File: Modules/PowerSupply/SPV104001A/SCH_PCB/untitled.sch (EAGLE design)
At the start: 24 parts, among them X2 SROUB3M, X3 SROUB3M, X4 SROUB3M, X5 SROUB3M

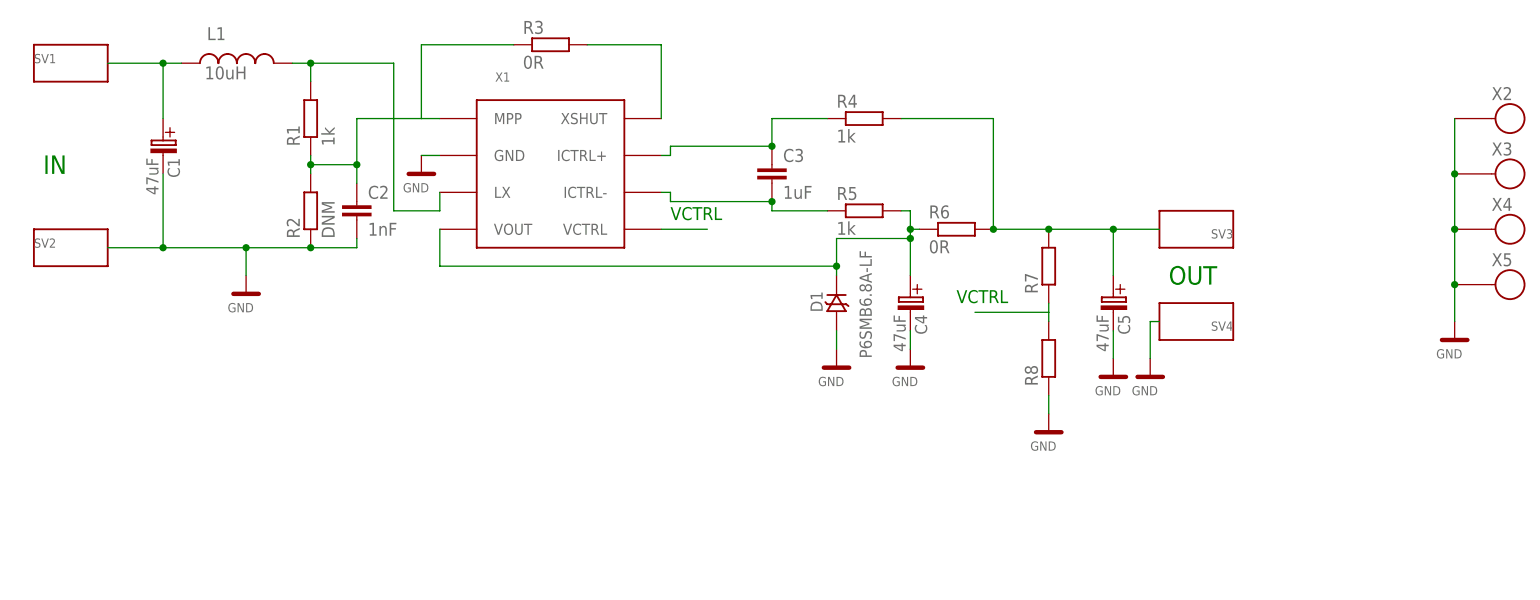
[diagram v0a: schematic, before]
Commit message: 
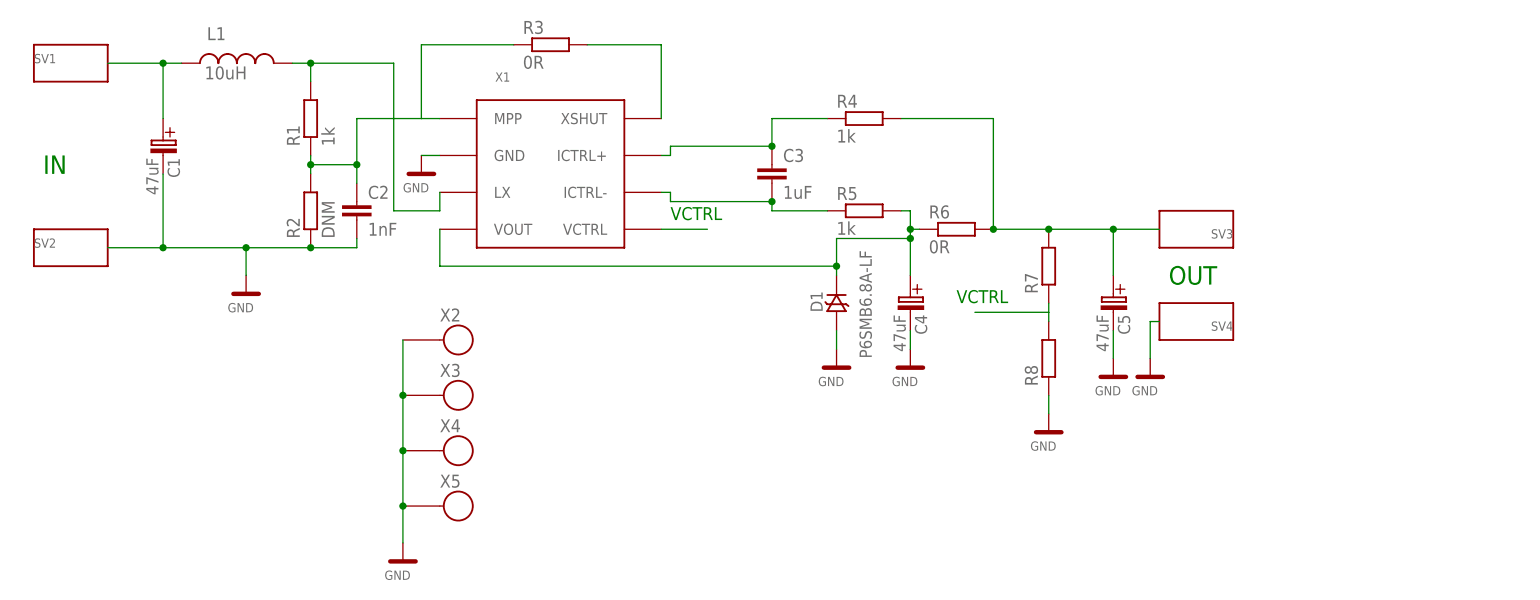
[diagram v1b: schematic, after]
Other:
- moved on the sheet: X2, X3, X4, X5
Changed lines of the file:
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@@
 <setting verticaltext="up"/>
 </settings>
-<grid distance="0.05" unitdist="inch" unit="inch" style="lines" multiple="1" display="no" altdistance="0.01" altunitdist="inch" altunit="inch"/>
+<grid distance="0.1" unitdist="inch" unit="inch" style="lines" multiple="1" display="no" altdistance="0.01" altunitdist="inch" altunit="inch"/>
 <layers>
-<layer number="1" name="Top" color="4" fill="1" visible="yes" active="no"/>
-<layer number="16" name="Bottom" color="1" fill="1" visible="yes" active="no"/>
-<layer number="17" name="Pads" color="2" fill="1" visible="yes" active="no"/>
-<layer number="18" name="Vias" color="2" fill="1" visible="yes" active="no"/>
-<layer number="19" name="Unrouted" color="6" fill="1" visible="yes" active="no"/>
-<layer number="20" name="Dimension" color="15" fill="1" visible="yes" active="no"/>
-<layer number="21" name="tPlace" color="7" fill="1" visible="yes" active="no"/>
-<layer number="22" name="bPlace" color="7" fill="1" visible="yes" active="no"/>
-<layer number="23" name="tOrigins" color="15" fill="1" visible="yes" active="no"/>
-<layer number="24" name="bOrigins" color="15" fill="1" visible="yes" active="no"/>
-<layer number="25" name="tNames" color="7" fill="1" visible="yes" active="no"/>
-<layer number="26" name="bNames" color="7" fill="1" visible="yes" active="no"/>
-<layer number="27" name="tValues" color="7" fill="1" visible="yes" active="no"/>
-<layer number="28" name="bValues" color="7" fill="1" visible="yes" active="no"/>
+<layer number="1" name="Top" color="4" fill="1" visible="no" active="no"/>
+<layer number="16" name="Bottom" color="1" fill="1" visible="no" active="no"/>
+<layer number="17" name="Pads" color="2" fill="1" visible="no" active="no"/>
+<layer number="18" name="Vias" color="2" fill="1" visible="no" active="no"/>
+<layer number="19" name="Unrouted" color="6" fill="1" visible="no" active="no"/>
+<layer number="20" name="Dimension" color="15" fill="1" visible="no" active="no"/>
+<layer number="21" name="tPlace" color="7" fill="1" visible="no" active="no"/>
+<layer number="22" name="bPlace" color="7" fill="1" visible="no" active="no"/>
+<layer number="23" name="tOrigins" color="15" fill="1" visible="no" active="no"/>
+<layer number="24" name="bOrigins" color="15" fill="1" visible="no" active="no"/>
+<layer number="25" name="tNames" color="7" fill="1" visible="no" active="no"/>
+<layer number="26" name="bNames" color="7" fill="1" visible="no" active="no"/>
+<layer number="27" name="tValues" color="7" fill="1" visible="no" active="no"/>
+<layer number="28" name="bValues" color="7" fill="1" visible="no" active="no"/>
 <layer number="29" name="tStop" color="7" fill="3" visible="no" active="no"/>
 <layer number="30" name="bStop" color="7" fill="6" visible="no" active="no"/>
@@
 <layer number="35" name="tGlue" color="7" fill="4" visible="no" active="no"/>
 <layer number="36" name="bGlue" color="7" fill="5" visible="no" active="no"/>
-<layer number="37" name="tTest" color="7" fill="1" visible="yes" active="no"/>
-<layer number="38" name="bTest" color="7" fill="1" visible="yes" active="no"/>
+<layer number="37" name="tTest" color="7" fill="1" visible="no" active="no"/>
+<layer number="38" name="bTest" color="7" fill="1" visible="no" active="no"/>
 <layer number="39" name="tKeepout" color="4" fill="11" visible="no" active="no"/>
 <layer number="40" name="bKeepout" color="1" fill="11" visible="no" active="no"/>
@@
 <layer number="44" name="Drills" color="7" fill="1" visible="no" active="no"/>
 <layer number="45" name="Holes" color="7" fill="1" visible="no" active="no"/>
-<layer number="46" name="Milling" color="3" fill="1" visible="yes" active="no"/>
-<layer number="47" name="Measures" color="7" fill="1" visible="yes" active="no"/>
-<layer number="48" name="Document" color="7" fill="1" visible="yes" active="no"/>
-<layer number="49" name="Reference" color="7" fill="1" visible="yes" active="no"/>
-<layer number="50" name="dxf" color="7" fill="1" visible="yes" active="no"/>
-<layer number="51" name="tDocu" color="7" fill="1" visible="yes" active="no"/>
-<layer number="52" name="bDocu" color="7" fill="1" visible="yes" active="no"/>
-<layer number="53" name="tPadExt" color="7" fill="1" visible="yes" active="no"/>
-<layer number="54" name="bPadExt" color="1" fill="1" visible="yes" active="no"/>
-<layer number="56" name="wert" color="7" fill="1" visible="yes" active="no"/>
+<layer number="46" name="Milling" color="3" fill="1" visible="no" active="no"/>
+<layer number="47" name="Measures" color="7" fill="1" visible="no" active="no"/>
+<layer number="48" name="Document" color="7" fill="1" visible="no" active="no"/>
+<layer number="49" name="Reference" color="7" fill="1" visible="no" active="no"/>
+<layer number="50" name="dxf" color="7" fill="1" visible="no" active="no"/>
+<layer number="51" name="tDocu" color="7" fill="1" visible="no" active="no"/>
+<layer number="52" name="bDocu" color="7" fill="1" visible="no" active="no"/>
+<layer number="53" name="tPadExt" color="7" fill="1" visible="no" active="no"/>
+<layer number="54" name="bPadExt" color="1" fill="1" visible="no" active="no"/>
+<layer number="56" name="wert" color="7" fill="1" visible="no" active="no"/>
 <layer number="91" name="Nets" color="2" fill="1" visible="yes" active="yes"/>
 <layer number="92" name="Busses" color="1" fill="1" visible="yes" active="yes"/>
@@
 <instance part="GND6" gate="G$1" x="77.47" y="17.78"/>
 <instance part="GND7" gate="G$1" x="82.55" y="17.78"/>
-<instance part="X2" gate="P4" x="132.08" y="50.8"/>
-<instance part="X3" gate="P4" x="132.08" y="43.18"/>
-<instance part="X4" gate="P4" x="132.08" y="35.56"/>
-<instance part="X5" gate="P4" x="132.08" y="27.94"/>
-<instance part="GND8" gate="G$1" x="124.46" y="22.86"/>
+<instance part="X2" gate="P4" x="-12.7" y="20.32"/>
+<instance part="X3" gate="P4" x="-12.7" y="12.7"/>
+<instance part="X4" gate="P4" x="-12.7" y="5.08"/>
+<instance part="X5" gate="P4" x="-12.7" y="-2.54"/>
+<instance part="GND8" gate="G$1" x="-20.32" y="-7.62"/>
 <instance part="R6" gate="G$1" x="55.88" y="35.56"/>
 <instance part="R3" gate="G$1" x="0" y="60.96"/>
@@
 <segment>
 <pinref part="X2" gate="P4" pin="P$1"/>
-<wire x1="124.46" y1="50.8" x2="124.46" y2="43.18" width="0.1524" layer="91"/>
+<wire x1="-20.32" y1="20.32" x2="-20.32" y2="12.7" width="0.1524" layer="91"/>
 <pinref part="X3" gate="P4" pin="P$1"/>
-<junction x="124.46" y="43.18"/>
-<wire x1="124.46" y1="43.18" x2="124.46" y2="35.56" width="0.1524" layer="91"/>
+<junction x="-20.32" y="12.7"/>
+<wire x1="-20.32" y1="12.7" x2="-20.32" y2="5.08" width="0.1524" layer="91"/>
 <pinref part="X4" gate="P4" pin="P$1"/>
-<junction x="124.46" y="35.56"/>
-<wire x1="124.46" y1="35.56" x2="124.46" y2="27.94" width="0.1524" layer="91"/>
+<junction x="-20.32" y="5.08"/>
+<wire x1="-20.32" y1="5.08" x2="-20.32" y2="-2.54" width="0.1524" layer="91"/>
 <pinref part="X5" gate="P4" pin="P$1"/>
-<junction x="124.46" y="27.94"/>
-<wire x1="124.46" y1="27.94" x2="124.46" y2="22.86" width="0.1524" layer="91"/>
+<junction x="-20.32" y="-2.54"/>
+<wire x1="-20.32" y1="-2.54" x2="-20.32" y2="-7.62" width="0.1524" layer="91"/>
 <pinref part="GND8" gate="G$1" pin="GND"/>
 </segment>

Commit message: 
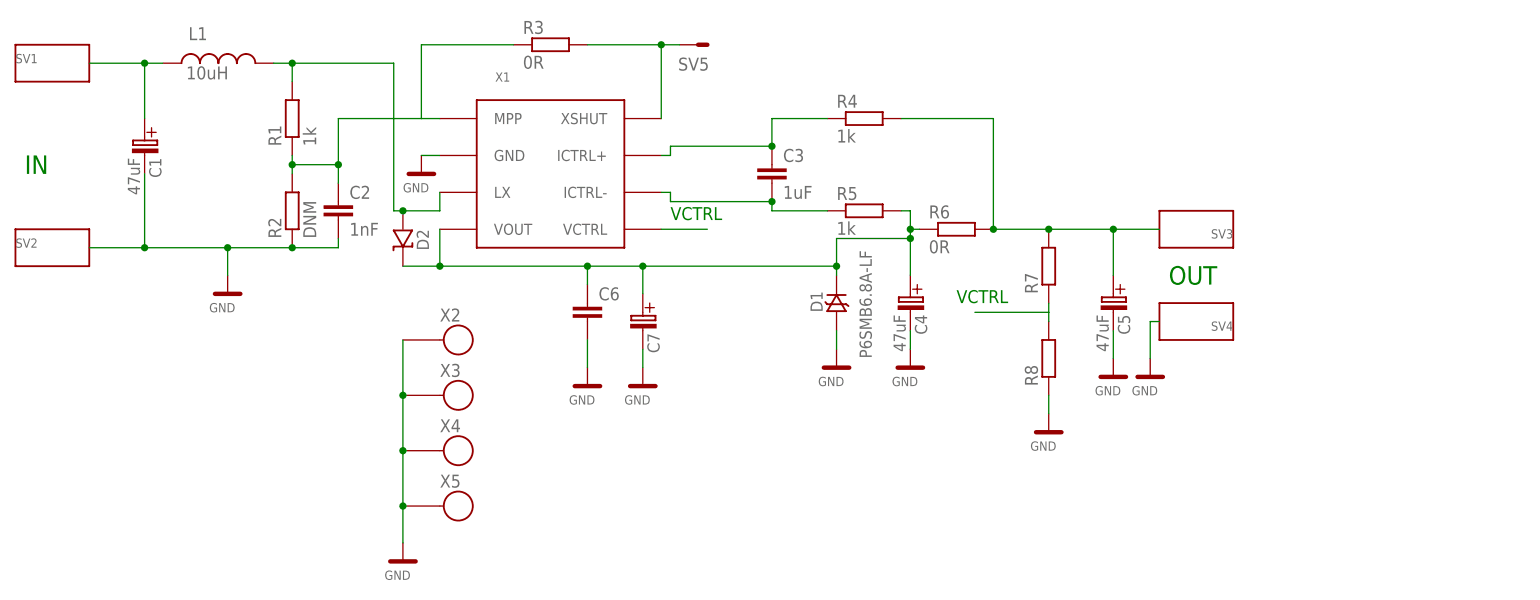
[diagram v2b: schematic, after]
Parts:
- added C6: (no value), moje_C:C0805
- added C7: (no value), moje_C:B
- added D2: (no value), moje_diody:D-SHOTKY-SMA
- added SV5: (no value), moje_hrebinky:MA01-1
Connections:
- net GND: now also C6.2, C7.C_EL-
- net N$2: now also SV5.P$1
- net N$5: now also C6.1, C7.C_EL+, D2.K
- net N$6: now also D2.A
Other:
- moved on the sheet: C1, C2, L1, R1, R2, SV1, SV2
